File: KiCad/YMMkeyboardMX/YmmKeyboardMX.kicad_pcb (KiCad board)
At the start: 2 copper layers, 215.9 x 123.8 mm, 73 parts, among them SW1 SW_Push, SW10 SW_Push, SW11 SW_Push, SW12 SW_Push, SW13 SW_Push, SW14 SW_Push, SW15 SW_Push, SW16 SW_Push, SW17 SW_Push, SW18 SW_Push, SW19 SW_Push, SW2 SW_Push, SW20 SW_Push, SW21 SW_Push, SW22 SW_Push, SW23 SW_Push, SW24 SW_Push, SW25 SW_Push, SW26 SW_Push, SW27 SW_Push, SW28 SW_Push, SW29 SW_Push, SW3 SW_Push, SW30 SW_Push, SW31 RotaryEncoder_Switch, SW4 SW_Push, SW5 SW_Push, SW6 SW_Push, SW7 SW_Push, SW8 SW_Push, SW9 SW_Push, U1 RP2040-Zero

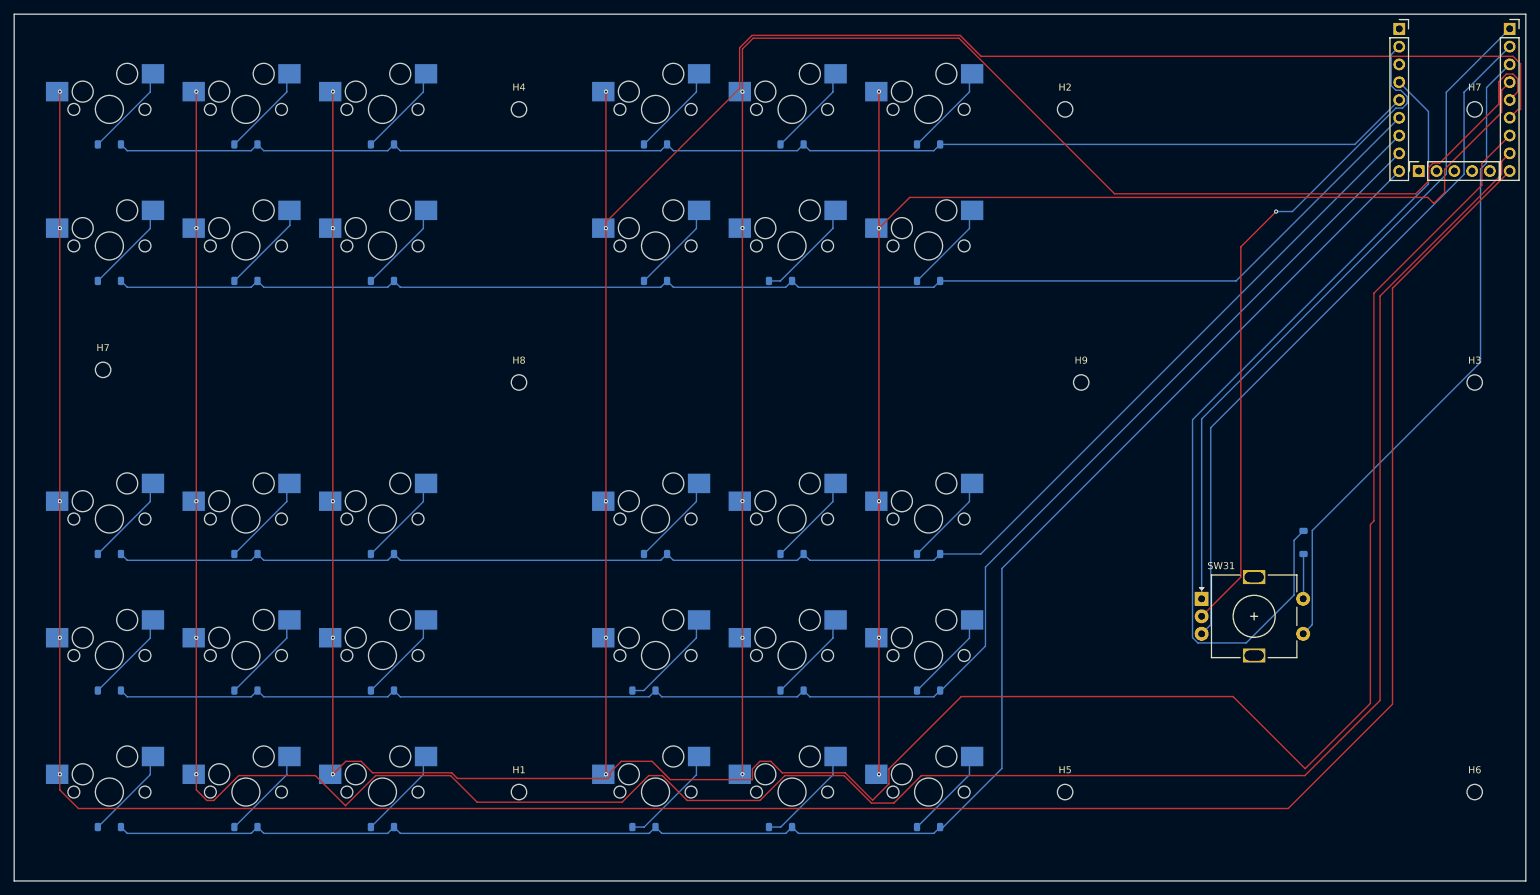
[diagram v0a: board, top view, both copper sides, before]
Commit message: ねじを締めたときに断線しそうなので修正
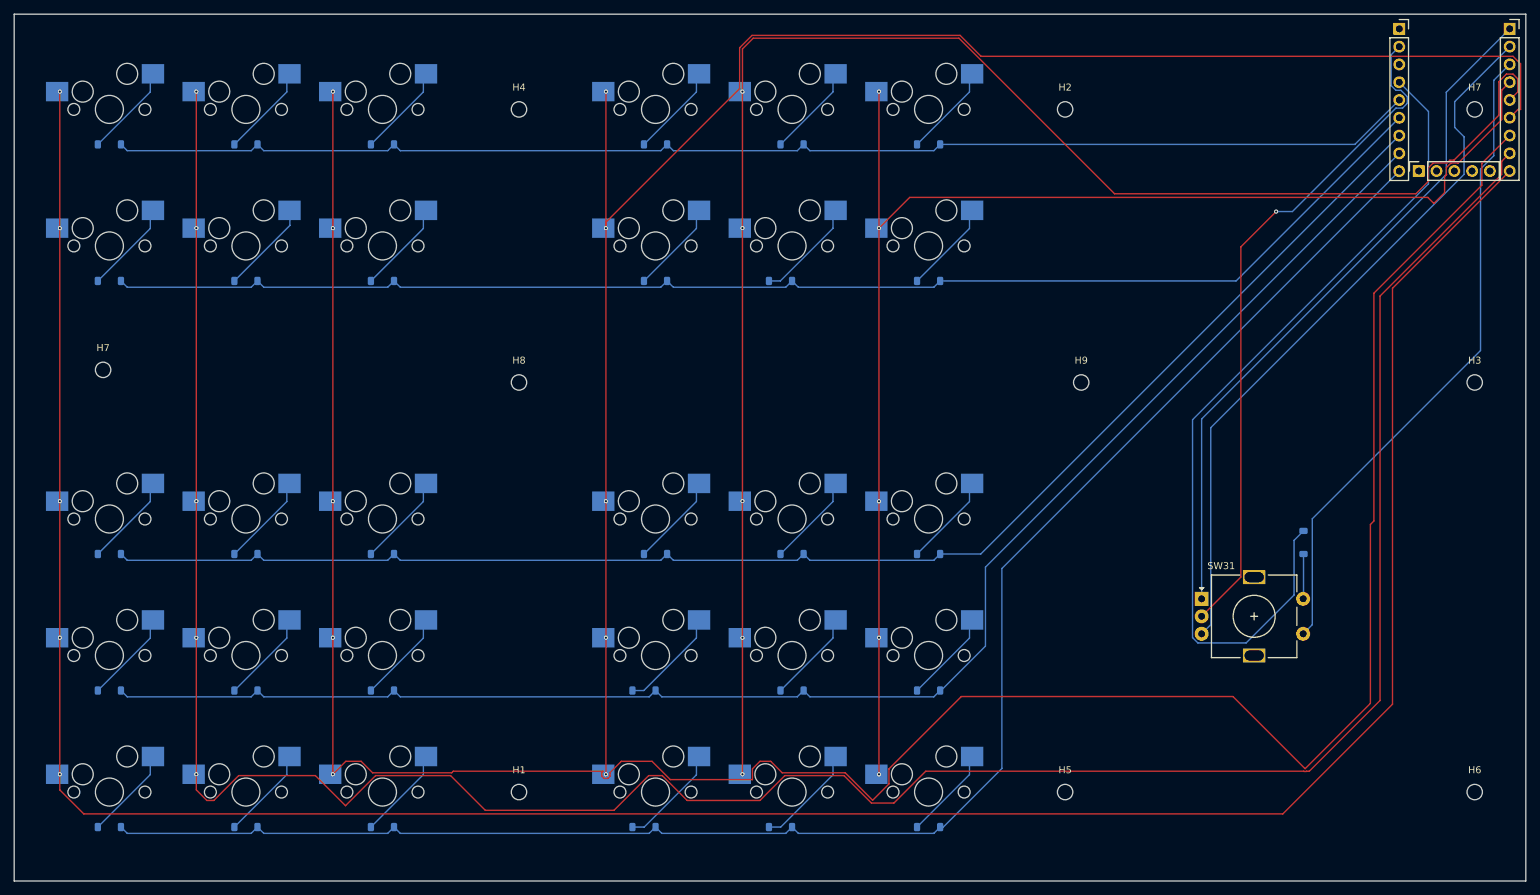
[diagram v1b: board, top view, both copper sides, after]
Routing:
- net Net-(SW31-PadB): track 102.1 -> 103.2 mm
- net Net-(SW14-Pad1): track 374.1 -> 375.1 mm
- net Net-(SW11-Pad1): track 238.0 -> 239.0 mm
- net Net-(SW15-Pad1): track 359.0 -> 359.9 mm
- net Net-(SW12-Pad1): track 200.7 -> 201.4 mm
- net Net-(SW1-Pad1): track 380.4 -> 381.1 mm
